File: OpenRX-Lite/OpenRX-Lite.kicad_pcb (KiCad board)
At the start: 6 copper layers, 8.5 x 12.3 mm, 39 parts, among them U1 ESP32-C3FH4, U2 TLV75533PDQNR, U3 SX1281IMLTRT, X1 CJ17-400001010B20

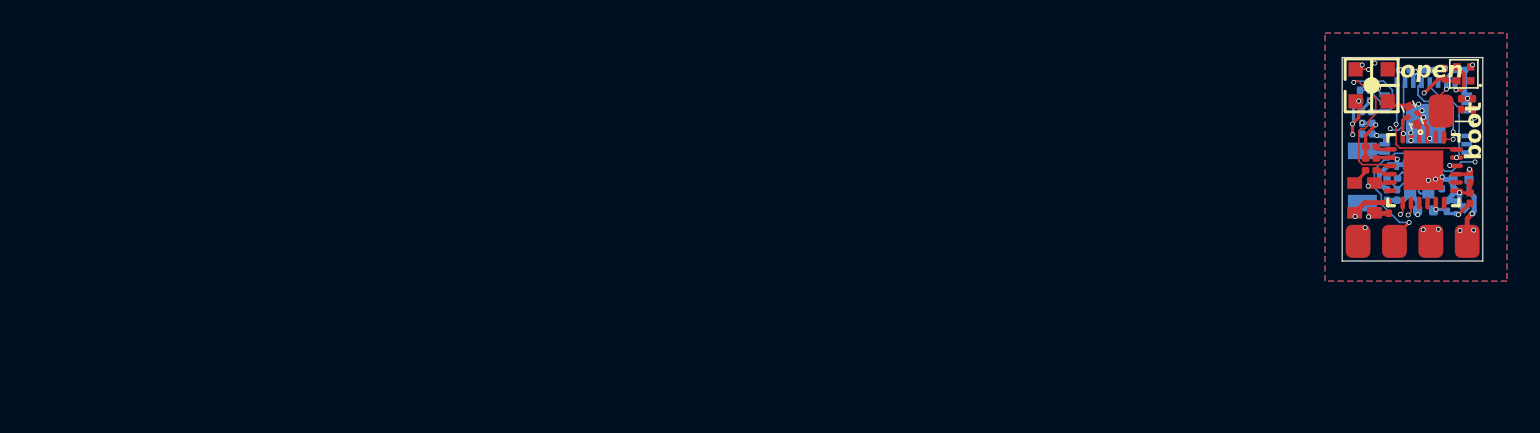
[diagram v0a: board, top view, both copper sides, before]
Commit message: OpenRX Lite (UFL + molex)
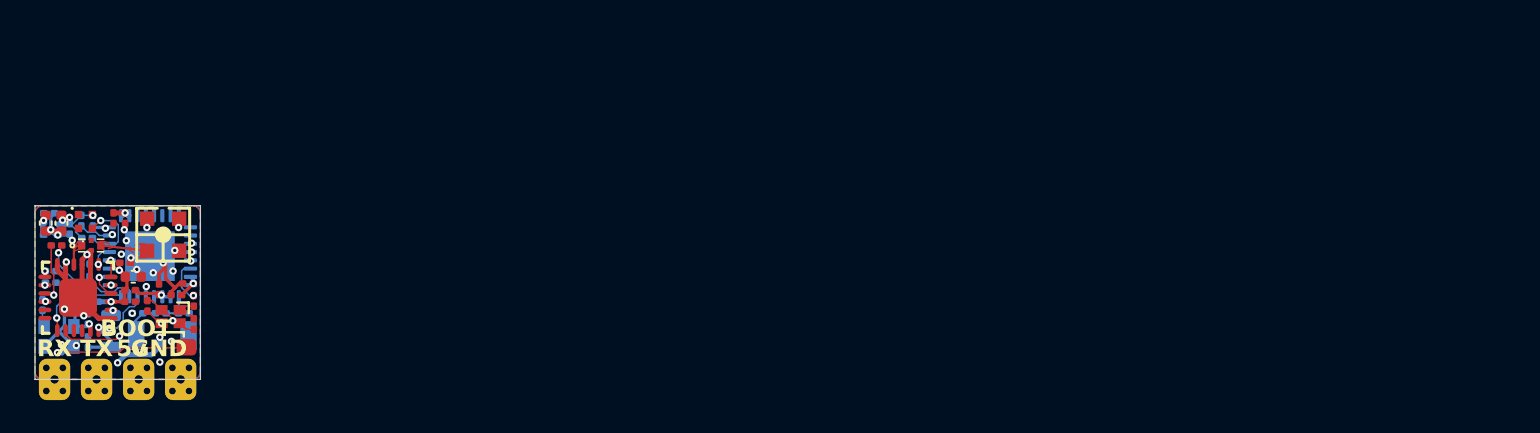
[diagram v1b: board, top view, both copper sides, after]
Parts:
- removed C18, C7: 100nF, Capacitor_SMD:C_0201_0603Metric
- removed C2: 1uF, Capacitor_SMD:C_0201_0603Metric
- removed R1: 10k, Resistor_SMD:R_0201_0603Metric
- added C21: 1.2pF, Capacitor_SMD:C_0201_0603Metric, B.Cu at (106.2, 106.0)
- added C22: 1.2pF, Capacitor_SMD:C_0201_0603Metric, B.Cu at (109.0, 106.0)
- added C23: 1uF, Capacitor_SMD:C_0201_0603Metric, F.Cu at (105.5, 100.2)
- added C24: 10nF, Capacitor_SMD:C_0201_0603Metric, F.Cu at (109.2, 104.2)
- added C25: 1uF, Capacitor_SMD:C_0201_0603Metric, F.Cu at (107.5, 104.5)
- added C26: 10nF, Capacitor_SMD:C_0201_0603Metric, B.Cu at (101.0, 104.2)
- added C27: 10nF, Capacitor_SMD:C_0201_0603Metric, B.Cu at (101.0, 103.5)
- added C28: 1uF, Capacitor_SMD:C_0201_0603Metric, B.Cu at (103.3, 102.7)
- added L2: 2.5nH, Inductor_SMD:L_0201_0603Metric, B.Cu at (107.6, 106.0)
- added L3: 2.0nH, Inductor_SMD:L_0201_0603Metric, F.Cu at (105.8, 104.6)
- added L4: 15uH, Inductor_SMD:L_0805_2012Metric, B.Cu at (104.6, 107.1)
- added R5: 10k, Resistor_SMD:R_0201_0603Metric, B.Cu at (103.3, 104.1)
- C1, C3: value 18pF -> 15pF; moved to F.Cu
- C11: value 100nF -> 10uF; footprint Capacitor_SMD:C_0201_0603Metric -> Capacitor_SMD:C_0402_1005Metric
- C13, C14, C17, C19, C20, OSC1: moved to B.Cu
- C16, C4, C5, C6, C8, L1, R2, X1: moved to F.Cu
- TP5: value GND -> BOOT
- U1: value ESP32-C3FH4 -> ESP32-C3; footprint OpenRX-Shared:QFN-32_L5.0-W5.0-P0.50-TL-EP3.7 -> Package_DFN_QFN:QFN-32-1EP_5x5mm_P0.5mm_EP3.7x3.7mm
- moved C8 85.6 mm to (100.7, 100.5), turned to -90 degrees
- moved C10 85.6 mm to (100.8, 100.0), turned to 0 degrees
- moved U2 85.5 mm to (101.0, 101.0), turned to 180 degrees
- moved D1 83.8 mm to (103.0, 100.5), turned to 0 degrees
- moved R4 83.8 mm to (102.8, 100.4), turned to -90 degrees
- moved C17 83.6 mm to (103.5, 105.3), turned to 180 degrees
- moved C15 83.3 mm to (102.1, 100.9), turned to -90 degrees
- moved C16 82.5 mm to (101.6, 100.5), turned to -90 degrees
- moved C9 82.1 mm to (105.8, 105.3), turned to 0 degrees
- moved R3 81.7 mm to (103.2, 101.5)
- moved U3 81.7 mm to (102.6, 105.0)
- moved C11 81.0 mm to (105.9, 103.8), turned to 0 degrees
- moved TP3 80.8 mm to (106.3, 110.0), turned to 0 degrees
- moved C19 80.7 mm to (100.5, 105.5), turned to 90 degrees
- moved FL1 80.3 mm to (103.4, 101.9), turned to 0 degrees
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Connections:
- net /ESP32-C3 + SX1281 Core/BUSY renamed /ESP32-C3 + SX1281 Core (UFL)/BUSY
- net /ESP32-C3 + SX1281 Core/CHIP_BOOT renamed /ESP32-C3 + SX1281 Core (UFL)/BOOT
- net /ESP32-C3 + SX1281 Core/RST renamed /ESP32-C3 + SX1281 Core (UFL)/RST
- net /ESP32-C3 + SX1281 Core/XTAL_N renamed /ESP32-C3 + SX1281 Core (UFL)/XTAL_N
- net /ESP32-C3 + SX1281 Core/XTAL_P renamed /ESP32-C3 + SX1281 Core (UFL)/XTAL_P
- AE1 pad 1: /ESP32-C3 + SX1281 Core/WIFI -> /ESP32-C3 + SX1281 Core (UFL)/WIFI
- AE2 pad 4: unconnected-(AE2-Pad4) -> GND
- C20 pad 1: Net-(U3-VR_PA) -> GND
- C20 pad 2: GND -> Net-(U3-DCC_FB)
- D1 pad 2: +5V -> +3V3
- D1 pad 4: /ESP32-C3 + SX1281 Core/LED -> /ESP32-C3 + SX1281 Core (UFL)/LED
- R3 pad 2: /ESP32-C3 + SX1281 Core/NSS -> /ESP32-C3 + SX1281 Core (UFL)/LED
- U1 pad 1: /ESP32-C3 + SX1281 Core/WIFI -> Net-(U1-LNA_IN)
- U1 pad 10: /ESP32-C3 + SX1281 Core/DIO1 -> /ESP32-C3 + SX1281 Core (UFL)/MISO
- U1 pad 12: /ESP32-C3 + SX1281 Core/MISO -> /ESP32-C3 + SX1281 Core (UFL)/SCK
- U1 pad 13: /ESP32-C3 + SX1281 Core/MOSI -> /ESP32-C3 + SX1281 Core (UFL)/NSS
- U1 pad 14: /ESP32-C3 + SX1281 Core/NSS -> /ESP32-C3 + SX1281 Core (UFL)/LED
- U1 pad 16: /ESP32-C3 + SX1281 Core/LED -> GND
- U1 pad 2: +3V3 -> Net-(C25-Pad1)
- U1 pad 3: +3V3 -> Net-(C25-Pad1)
- U1 pad 7: /ESP32-C3 + SX1281 Core/CHIP_EN -> /ESP32-C3 + SX1281 Core (UFL)/CHIP_EN
- U1 pad 9: /ESP32-C3 + SX1281 Core/SCK -> /ESP32-C3 + SX1281 Core (UFL)/MOSI
- U3 pad 12: unconnected-(U3-DCC_FB-Pad12) -> Net-(U3-DCC_FB)
- U3 pad 14: unconnected-(U3-DCC_SW-Pad14) -> Net-(U3-DCC_SW)
- U3 pad 16: /ESP32-C3 + SX1281 Core/MISO -> /ESP32-C3 + SX1281 Core (UFL)/MISO
- U3 pad 17: /ESP32-C3 + SX1281 Core/MOSI -> /ESP32-C3 + SX1281 Core (UFL)/MOSI
- U3 pad 18: /ESP32-C3 + SX1281 Core/SCK -> /ESP32-C3 + SX1281 Core (UFL)/SCK
- U3 pad 19: /ESP32-C3 + SX1281 Core/NSS -> /ESP32-C3 + SX1281 Core (UFL)/NSS
- U3 pad 2: +3V3 -> Net-(U3-DCC_FB)
- U3 pad 5: GND -> unconnected-(U3-GND-Pad5)
- U3 pad 8: /ESP32-C3 + SX1281 Core/DIO1 -> /ESP32-C3 + SX1281 Core (UFL)/DIO1
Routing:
- net /ESP32-C3 + SX1281 Core (UFL)/BOOT: track 2.76 -> 19.5 mm, vias 1 -> 2
- net /ESP32-C3 + SX1281 Core/DIO1: track 10.0 -> 0.00 mm, vias 2 -> 0
- net GND: track 38.6 -> 30.2 mm, vias 28 -> 25
- net /ESP32-C3 + SX1281 Core (UFL)/DIO1: track 0.00 -> 8.20 mm, vias 0 -> 2
- net Net-(U3-DCC_FB): track 0.00 -> 7.68 mm, vias 0 -> 2
- net /ESP32-C3 + SX1281 Core/SCK: track 7.53 -> 0.00 mm, vias 1 -> 0
- net /ESP32-C3 + SX1281 Core/NSS: track 7.45 -> 0.00 mm, vias 2 -> 0
- net /ESP32-C3 + SX1281 Core/MISO: track 7.04 -> 0.00 mm, vias 2 -> 0
- net /ESP32-C3 + SX1281 Core/MOSI: track 5.63 -> 0.00 mm, vias 1 -> 0
- net /ESP32-C3 + SX1281 Core (UFL)/LED: track 0.00 -> 4.65 mm, vias 0 -> 1
- net /ESP32-C3 + SX1281 Core (UFL)/CHIP_EN: track 0.00 -> 4.21 mm
- net /ESP32-C3 + SX1281 Core (UFL)/BUSY: track 9.55 -> 5.50 mm, vias 2 -> 1
- net +5V: track 16.9 -> 13.7 mm, vias 4 -> 1
- net +3V3: track 19.8 -> 22.4 mm, vias 9 -> 11
- net /ESP32-C3 + SX1281 Core/LED: track 2.43 -> 0.00 mm, vias 1 -> 0
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- added copper zone on In2.Cu, net +3V3
- added copper zone on In3.Cu, net GND
- added copper zone on F.Cu, net Net-(FL1-IN)
- added copper zone on F.Cu, net Net-(FL1-OUT)
- removed copper zone on In3.Cu, net +3V3
- removed copper zone on In2.Cu, net GND
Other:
- board size 8.5 x 12.3 mm -> 10 x 10.5 mm
- board text added: "BOOT"
- board text removed: "boot"
